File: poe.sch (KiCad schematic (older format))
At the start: 15 parts

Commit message: am Routing rumgespielt
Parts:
- 1.65k1, 1.65k2: renamed from 1.65kΩ; footprint (none) -> Resistors_ThroughHole:Resistor_Horizontal_RM20mm
- D1, D2: renamed from D?; footprint (none) -> Diodes_ThroughHole:Diode_DO-35_SOD27_Horizontal_RM10
- D10, D7, D8, D9: renamed from D?; footprint (none) -> LEDs:LED-3MM
- D3, D4, D5, D6: renamed from D?; footprint (none) -> Discret:D3
- P1: renamed from P?; footprint (none) -> Pin_Headers:Pin_Header_Angled_1x08
- R1, R2: renamed from R; footprint (none) -> Resistors_ThroughHole:Resistor_Horizontal_RM7mm
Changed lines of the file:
@@
 $EndDescr
 $Comp
-L CONN_01X08 P?
+L CONN_01X08 P1
 U 1 1 589CD597
 P 3300 3150
-F 0 "P?" H 3300 3600 50  0000 C CNN
+F 0 "P1" H 3300 3600 50  0000 C CNN
 F 1 "CONN_01X08" V 3400 3150 50  0000 C CNN
-F 2 "" H 3300 3150 50  0000 C CNN
+F 2 "Pin_Headers:Pin_Header_Angled_1x08" H 3300 3150 50  0001 C CNN
 F 3 "" H 3300 3150 50  0000 C CNN
 	1    3300 3150
@@
 $EndComp
 $Comp
-L R R
+L R R1
 U 1 1 589CD7AC
 P 5500 3050
-F 0 "R" V 5580 3050 50  0000 C CNN
+F 0 "R1" V 5580 3050 50  0000 C CNN
 F 1 "22kΩ" V 5500 3050 50  0000 C CNN
-F 2 "" V 5430 3050 50  0000 C CNN
+F 2 "Resistors_ThroughHole:Resistor_Horizontal_RM7mm" V 5430 3050 50  0001 C CNN
 F 3 "" H 5500 3050 50  0000 C CNN
 	1    5500 3050
@@
 $EndComp
 $Comp
-L R R
+L R R2
 U 1 1 589CD7FF
 P 5500 3800
-F 0 "R" V 5580 3800 50  0000 C CNN
+F 0 "R2" V 5580 3800 50  0000 C CNN
 F 1 "22kΩ" V 5500 3800 50  0000 C CNN
-F 2 "" V 5430 3800 50  0000 C CNN
+F 2 "Resistors_ThroughHole:Resistor_Horizontal_RM7mm" V 5430 3800 50  0001 C CNN
 F 3 "" H 5500 3800 50  0000 C CNN
 	1    5500 3800
@@
 $EndComp
 $Comp
-L ZENER D?
+L ZENER D4
 U 1 1 589CDF37
 P 5700 4000
-F 0 "D?" H 5700 4100 50  0000 C CNN
+F 0 "D4" H 5700 4100 50  0000 C CNN
 F 1 "ZENER" H 5700 3900 50  0000 C CNN
-F 2 "" H 5700 4000 50  0000 C CNN
+F 2 "Discret:D3" H 5700 4000 50  0001 C CNN
 F 3 "" H 5700 4000 50  0000 C CNN
 	1    5700 4000
@@
 $EndComp
 $Comp
-L ZENER D?
+L ZENER D6
 U 1 1 589CE16F
 P 6100 4000
-F 0 "D?" H 6100 4100 50  0000 C CNN
+F 0 "D6" H 6100 4100 50  0000 C CNN
 F 1 "ZENER" H 6100 3900 50  0000 C CNN
-F 2 "" H 6100 4000 50  0000 C CNN
+F 2 "Discret:D3" H 6100 4000 50  0001 C CNN
 F 3 "" H 6100 4000 50  0000 C CNN
 	1    6100 4000
@@
 $EndComp
 $Comp
-L ZENER D?
+L ZENER D3
 U 1 1 589CE1DE
 P 5700 2850
-F 0 "D?" H 5700 2950 50  0000 C CNN
+F 0 "D3" H 5700 2950 50  0000 C CNN
 F 1 "ZENER" H 5700 2750 50  0000 C CNN
-F 2 "" H 5700 2850 50  0000 C CNN
+F 2 "Discret:D3" H 5700 2850 50  0001 C CNN
 F 3 "" H 5700 2850 50  0000 C CNN
 	1    5700 2850
@@
 $EndComp
 $Comp
-L ZENER D?
+L ZENER D5
 U 1 1 589CE247
 P 6100 2850
-F 0 "D?" H 6100 2950 50  0000 C CNN
+F 0 "D5" H 6100 2950 50  0000 C CNN
 F 1 "ZENER" H 6100 2750 50  0000 C CNN
-F 2 "" H 6100 2850 50  0000 C CNN
+F 2 "Discret:D3" H 6100 2850 50  0001 C CNN
 F 3 "" H 6100 2850 50  0000 C CNN
 	1    6100 2850
@@
 $EndComp
 $Comp
-L R 1.65kΩ
+L R 1.65k1
 U 1 1 589CE2D4
 P 5750 3300
-F 0 "1.65kΩ" V 5830 3300 50  0000 C CNN
+F 0 "1.65k1" V 5830 3300 50  0000 C CNN
 F 1 "R" V 5750 3300 50  0000 C CNN
-F 2 "" V 5680 3300 50  0000 C CNN
+F 2 "Resistors_ThroughHole:Resistor_Horizontal_RM20mm" V 5680 3300 50  0001 C CNN
 F 3 "" H 5750 3300 50  0000 C CNN
 	1    5750 3300
@@
 $EndComp
 $Comp
-L R 1.65kΩ
+L R 1.65k2
 U 1 1 589CE307
 P 5750 3600
-F 0 "1.65kΩ" V 5830 3600 50  0000 C CNN
+F 0 "1.65k2" V 5830 3600 50  0000 C CNN
 F 1 "R" V 5750 3600 50  0000 C CNN
-F 2 "" V 5680 3600 50  0000 C CNN
+F 2 "Resistors_ThroughHole:Resistor_Horizontal_RM20mm" V 5680 3600 50  0001 C CNN
 F 3 "" H 5750 3600 50  0000 C CNN
 	1    5750 3600
@@
 $EndComp
 $Comp
-L LED D?
+L LED D8
 U 1 1 589CE453
 P 6300 3800
-F 0 "D?" H 6300 3900 50  0000 C CNN
+F 0 "D8" H 6300 3900 50  0000 C CNN
 F 1 "LED" H 6300 3700 50  0000 C CNN
-F 2 "" H 6300 3800 50  0000 C CNN
+F 2 "LEDs:LED-3MM" H 6300 3800 50  0001 C CNN
 F 3 "" H 6300 3800 50  0000 C CNN
 	1    6300 3800
@@
 $EndComp
 $Comp
-L LED D?
+L LED D10
 U 1 1 589CE49E
 P 6600 3800
-F 0 "D?" H 6600 3900 50  0000 C CNN
+F 0 "D10" H 6600 3900 50  0000 C CNN
 F 1 "LED" H 6600 3700 50  0000 C CNN
-F 2 "" H 6600 3800 50  0000 C CNN
+F 2 "LEDs:LED-3MM" H 6600 3800 50  0001 C CNN
 F 3 "" H 6600 3800 50  0000 C CNN
 	1    6600 3800
@@
 $EndComp
 $Comp
-L LED D?
+L LED D7
 U 1 1 589CE770
 P 6300 3050
-F 0 "D?" H 6300 3150 50  0000 C CNN
+F 0 "D7" H 6300 3150 50  0000 C CNN
 F 1 "LED" H 6300 2950 50  0000 C CNN
-F 2 "" H 6300 3050 50  0000 C CNN
+F 2 "LEDs:LED-3MM" H 6300 3050 50  0001 C CNN
 F 3 "" H 6300 3050 50  0000 C CNN
 	1    6300 3050
@@
 $EndComp
 $Comp
-L LED D?
+L LED D9
 U 1 1 589CE7ED
 P 6600 3050
-F 0 "D?" H 6600 3150 50  0000 C CNN
+F 0 "D9" H 6600 3150 50  0000 C CNN
 F 1 "LED" H 6600 2950 50  0000 C CNN
-F 2 "" H 6600 3050 50  0000 C CNN
+F 2 "LEDs:LED-3MM" H 6600 3050 50  0001 C CNN
 F 3 "" H 6600 3050 50  0000 C CNN
 	1    6600 3050
@@
 	6600 2850 6300 2850
 $Comp
-L Diode_Bridge D?
+L Diode_Bridge D1
 U 1 1 58A4AC46
 P 4600 2900
-F 0 "D?" H 4350 3200 50  0000 C CNN
+F 0 "D1" H 4350 3200 50  0000 C CNN
 F 1 "Diode_Bridge" H 4950 2550 50  0000 C CNN
-F 2 "" H 4600 2900 50  0000 C CNN
+F 2 "Diodes_ThroughHole:Diode_DO-35_SOD27_Horizontal_RM10" H 4600 2900 50  0001 C CNN
 F 3 "" H 4600 2900 50  0000 C CNN
 	1    4600 2900
@@
 	3600 3100 3600 3200
 $Comp
-L Diode_Bridge D?
+L Diode_Bridge D2
 U 1 1 58A4B96E
 P 4600 3800
-F 0 "D?" H 4350 4100 50  0000 C CNN
+F 0 "D2" H 4350 4100 50  0000 C CNN
 F 1 "Diode_Bridge" H 4950 3450 50  0000 C CNN
-F 2 "" H 4600 3800 50  0000 C CNN
+F 2 "Diodes_ThroughHole:Diode_DO-35_SOD27_Horizontal_RM10" H 4600 3800 50  0001 C CNN
 F 3 "" H 4600 3800 50  0000 C CNN
 	1    4600 3800

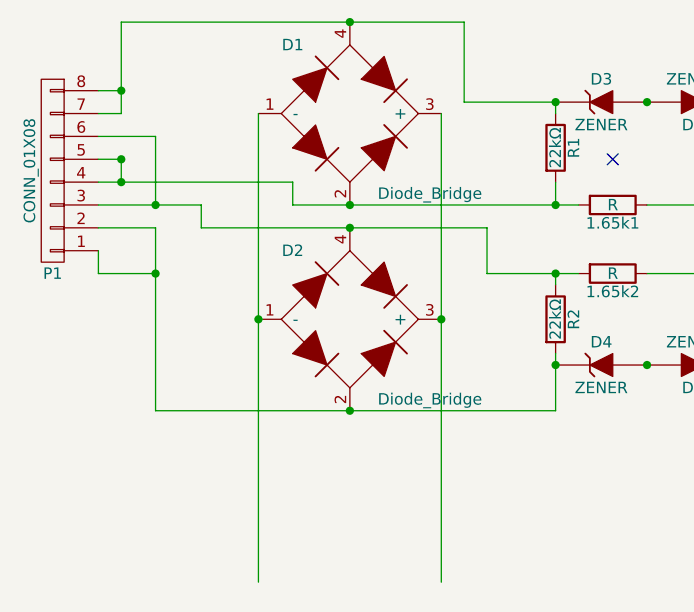
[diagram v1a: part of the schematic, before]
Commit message: Add NPN-MOSFET to output
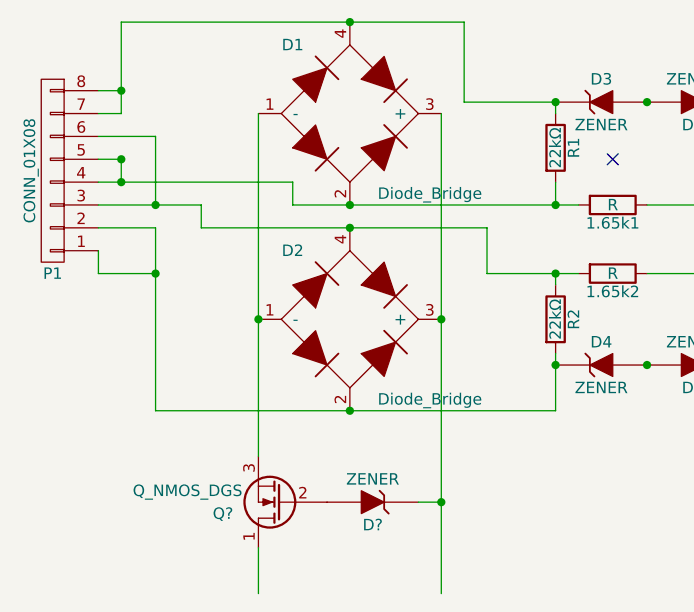
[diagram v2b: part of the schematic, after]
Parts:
- added D?: ZENER, symbol ZENER
- added Q?: Q_NMOS_DGS, symbol Q_NMOS_DGS
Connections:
- wire segments 35 -> 37
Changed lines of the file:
@@
 Wire Wire Line
 	3750 3600 3500 3600
-Wire Wire Line
-	4200 2900 4200 4950
-Wire Wire Line
-	5000 2900 5000 4950
 Connection ~ 4600 2500
 Connection ~ 4600 3300
@@
 Wire Wire Line
 	5500 3600 5500 3650
+$Comp
+L Q_NMOS_DGS Q?
+U 1 1 58B493A2
+P 4300 4600
+F 0 "Q?" H 4600 4650 50  0000 R CNN
+F 1 "Q_NMOS_DGS" H 4950 4550 50  0000 R CNN
+F 2 "" H 4500 4700 50  0000 C CNN
+F 3 "" H 4300 4600 50  0000 C CNN
+	1    4300 4600
+	-1   0    0    1
+$EndComp
+$Comp
+L ZENER D?
+U 1 1 58B4950D
+P 4700 4600
+F 0 "D?" H 4700 4700 50  0000 C CNN
+F 1 "ZENER" H 4700 4500 50  0000 C CNN
+F 2 "" H 4700 4600 50  0000 C CNN
+F 3 "" H 4700 4600 50  0000 C CNN
+	1    4700 4600
+	-1   0    0    1
+$EndComp
+Wire Wire Line
+	5000 4600 4900 4600
+Connection ~ 5000 4600
+Wire Wire Line
+	4200 4800 4200 5000
+Wire Wire Line
+	5000 2900 5000 5000
+Wire Wire Line
+	4200 2900 4200 4400
 $EndSCHEMATC

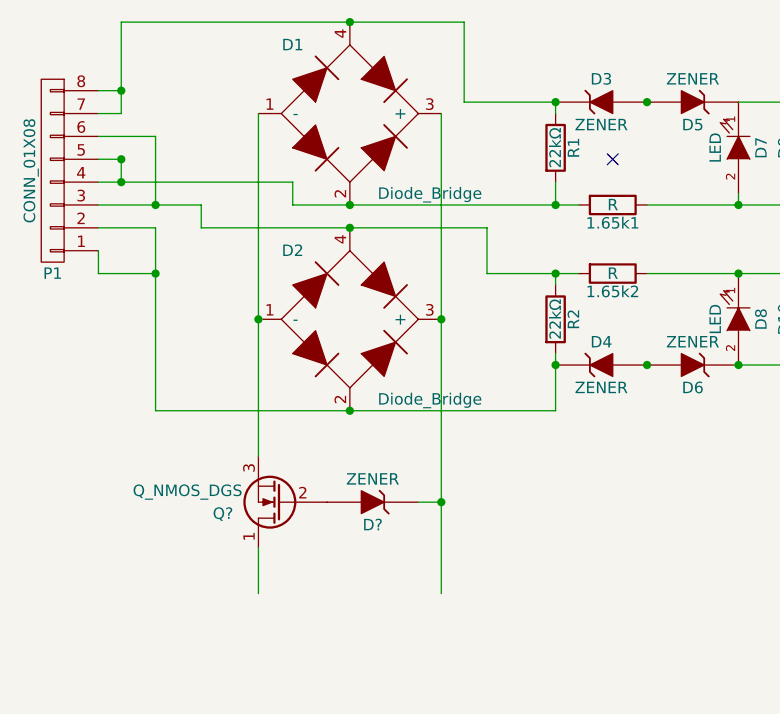
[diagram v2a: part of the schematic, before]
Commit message: +NMOS/Zener-enable load after classification
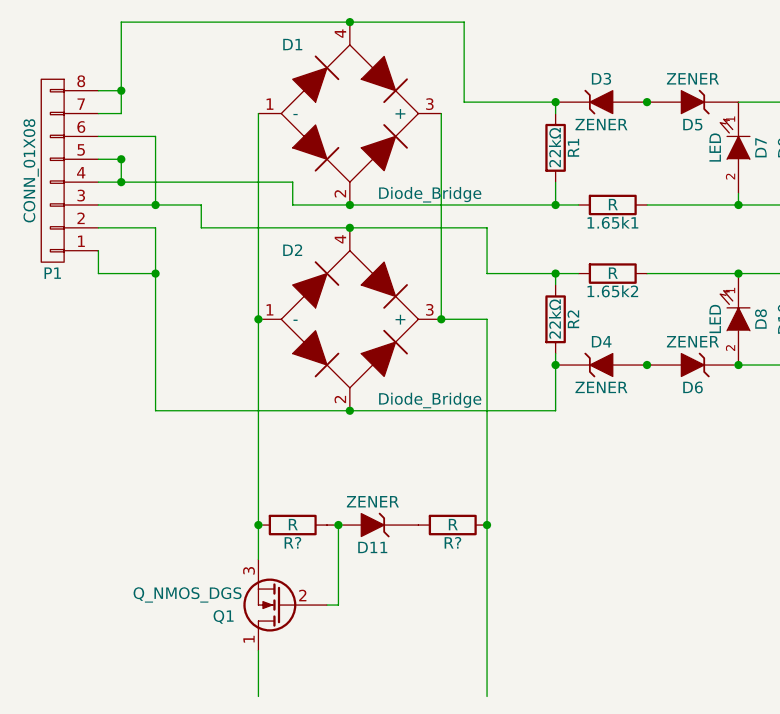
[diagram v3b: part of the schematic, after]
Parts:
- added R? (x2): R, symbol R
- gave numbers to parts that had none: 2
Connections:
- wire segments 37 -> 40
- no-connect marks 1 -> 0
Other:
- moved on the sheet: D11, Q1
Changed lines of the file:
@@
 Wire Wire Line
 	5200 3600 5200 3400
-NoConn ~ 5750 3100
 Wire Wire Line
 	5500 3300 5500 3200
@@
 	5500 3600 5500 3650
 $Comp
-L Q_NMOS_DGS Q?
+L Q_NMOS_DGS Q1
 U 1 1 58B493A2
-P 4300 4600
-F 0 "Q?" H 4600 4650 50  0000 R CNN
-F 1 "Q_NMOS_DGS" H 4950 4550 50  0000 R CNN
-F 2 "" H 4500 4700 50  0000 C CNN
-F 3 "" H 4300 4600 50  0000 C CNN
-	1    4300 4600
+P 4300 5050
+F 0 "Q1" H 4600 5100 50  0000 R CNN
+F 1 "Q_NMOS_DGS" H 4950 5000 50  0000 R CNN
+F 2 "" H 4500 5150 50  0000 C CNN
+F 3 "" H 4300 5050 50  0000 C CNN
+	1    4300 5050
 	-1   0    0    1
 $EndComp
 $Comp
-L ZENER D?
+L ZENER D11
 U 1 1 58B4950D
-P 4700 4600
-F 0 "D?" H 4700 4700 50  0000 C CNN
-F 1 "ZENER" H 4700 4500 50  0000 C CNN
-F 2 "" H 4700 4600 50  0000 C CNN
-F 3 "" H 4700 4600 50  0000 C CNN
-	1    4700 4600
+P 4700 4700
+F 0 "D11" H 4700 4800 50  0000 C CNN
+F 1 "ZENER" H 4700 4600 50  0000 C CNN
+F 2 "" H 4700 4700 50  0000 C CNN
+F 3 "" H 4700 4700 50  0000 C CNN
+	1    4700 4700
 	-1   0    0    1
 $EndComp
 Wire Wire Line
-	5000 4600 4900 4600
-Connection ~ 5000 4600
+	4200 5250 4200 5450
 Wire Wire Line
-	4200 4800 4200 5000
+	4200 2900 4200 4850
+$Comp
+L R R?
+U 1 1 58C46931
+P 4350 4700
+F 0 "R?" V 4430 4700 50  0000 C CNN
+F 1 "R" V 4350 4700 50  0000 C CNN
+F 2 "" V 4280 4700 50  0000 C CNN
+F 3 "" H 4350 4700 50  0000 C CNN
+	1    4350 4700
+	0    1    1    0
+$EndComp
+$Comp
+L R R?
+U 1 1 58C46A24
+P 5050 4700
+F 0 "R?" V 5130 4700 50  0000 C CNN
+F 1 "R" V 5050 4700 50  0000 C CNN
+F 2 "" V 4980 4700 50  0000 C CNN
+F 3 "" H 5050 4700 50  0000 C CNN
+	1    5050 4700
+	0    1    1    0
+$EndComp
 Wire Wire Line
-	5000 2900 5000 5000
+	5200 3800 5200 5450
 Wire Wire Line
-	4200 2900 4200 4400
+	5200 3800 5000 3800
+Wire Wire Line
+	5000 3800 5000 2900
+Wire Wire Line
+	4550 4700 4550 5050
+Wire Wire Line
+	4550 5050 4500 5050
+Connection ~ 5200 4700
+Connection ~ 4200 4700
+Connection ~ 4550 4700
 $EndSCHEMATC

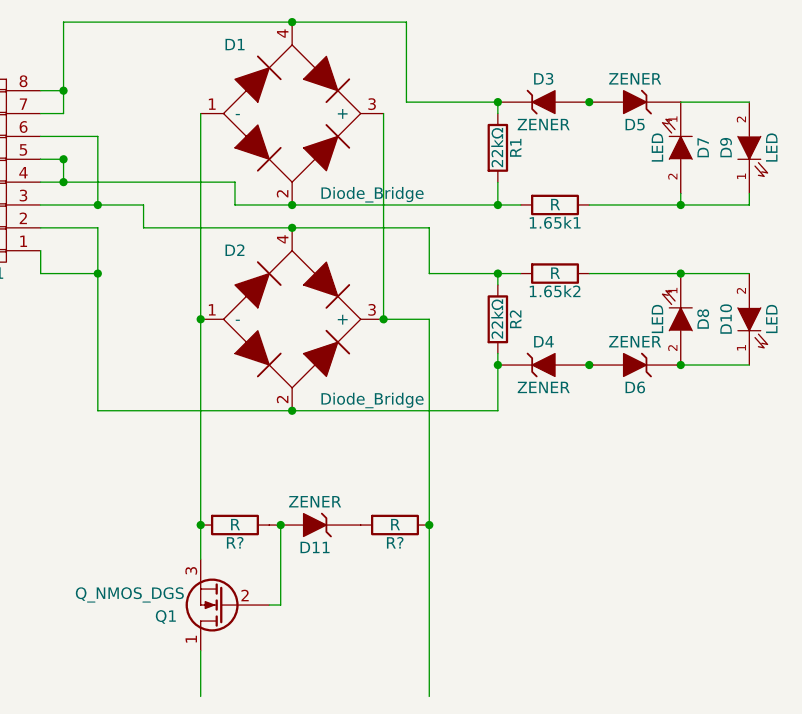
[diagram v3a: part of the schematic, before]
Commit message: widerstände vereinheitlicht
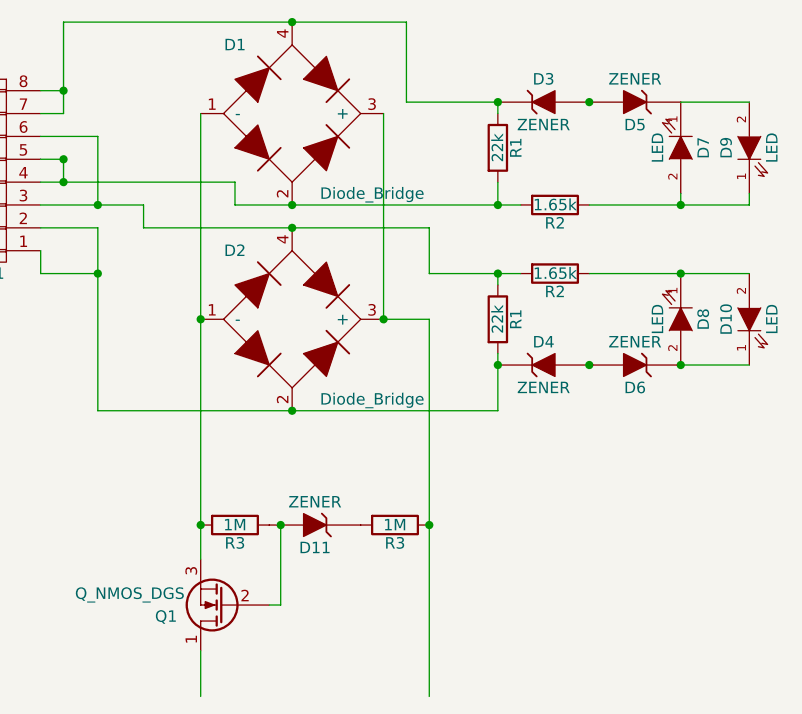
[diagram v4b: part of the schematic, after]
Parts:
- R1: value 22kΩ -> 22k
- R1: renamed from R2; value 22kΩ -> 22k
- R2: renamed from 1.65k1; value R -> 1.65k
- R2: renamed from 1.65k2; value R -> 1.65k
- R3: renamed from R?; value R -> 1M
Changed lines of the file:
@@
 P 5500 3050
 F 0 "R1" V 5580 3050 50  0000 C CNN
-F 1 "22kΩ" V 5500 3050 50  0000 C CNN
+F 1 "22k" V 5500 3050 50  0000 C CNN
 F 2 "Resistors_ThroughHole:Resistor_Horizontal_RM7mm" V 5430 3050 50  0001 C CNN
 F 3 "" H 5500 3050 50  0000 C CNN
@@
 $EndComp
 $Comp
-L R R2
+L R R1
 U 1 1 589CD7FF
 P 5500 3800
-F 0 "R2" V 5580 3800 50  0000 C CNN
-F 1 "22kΩ" V 5500 3800 50  0000 C CNN
+F 0 "R1" V 5580 3800 50  0000 C CNN
+F 1 "22k" V 5500 3800 50  0000 C CNN
 F 2 "Resistors_ThroughHole:Resistor_Horizontal_RM7mm" V 5430 3800 50  0001 C CNN
 F 3 "" H 5500 3800 50  0000 C CNN
@@
 $EndComp
 $Comp
-L R 1.65k1
+L R R2
 U 1 1 589CE2D4
 P 5750 3300
-F 0 "1.65k1" V 5830 3300 50  0000 C CNN
-F 1 "R" V 5750 3300 50  0000 C CNN
+F 0 "R2" V 5830 3300 50  0000 C CNN
+F 1 "1.65k" V 5750 3300 50  0000 C CNN
 F 2 "Resistors_ThroughHole:Resistor_Horizontal_RM20mm" V 5680 3300 50  0001 C CNN
 F 3 "" H 5750 3300 50  0000 C CNN
@@
 $EndComp
 $Comp
-L R 1.65k2
+L R R2
 U 1 1 589CE307
 P 5750 3600
-F 0 "1.65k2" V 5830 3600 50  0000 C CNN
-F 1 "R" V 5750 3600 50  0000 C CNN
+F 0 "R2" V 5830 3600 50  0000 C CNN
+F 1 "1.65k" V 5750 3600 50  0000 C CNN
 F 2 "Resistors_ThroughHole:Resistor_Horizontal_RM20mm" V 5680 3600 50  0001 C CNN
 F 3 "" H 5750 3600 50  0000 C CNN
@@
 	4200 2900 4200 4850
 $Comp
-L R R?
+L R R3
 U 1 1 58C46931
 P 4350 4700
-F 0 "R?" V 4430 4700 50  0000 C CNN
-F 1 "R" V 4350 4700 50  0000 C CNN
+F 0 "R3" V 4430 4700 50  0000 C CNN
+F 1 "1M" V 4350 4700 50  0000 C CNN
 F 2 "" V 4280 4700 50  0000 C CNN
 F 3 "" H 4350 4700 50  0000 C CNN
@@
 $EndComp
 $Comp
-L R R?
+L R R3
 U 1 1 58C46A24
 P 5050 4700
-F 0 "R?" V 5130 4700 50  0000 C CNN
-F 1 "R" V 5050 4700 50  0000 C CNN
+F 0 "R3" V 5130 4700 50  0000 C CNN
+F 1 "1M" V 5050 4700 50  0000 C CNN
 F 2 "" V 4980 4700 50  0000 C CNN
 F 3 "" H 5050 4700 50  0000 C CNN

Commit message: Stuff… Much Stuff…
(i know this commit is bad… but it would have been necessary ages ago)
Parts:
- removed D10, D9: LED, LEDs:LED-3MM, symbol LED
- removed P1: CONN_01X08, Pin_Headers:Pin_Header_Angled_1x08, symbol CONN_01X08
- removed Q1: Q_NMOS_DGS, symbol Q_NMOS_DGS
- added C1: >= 450 µF, Discret:C2V8, symbol CP
- added J1: RJ45, Connect:RJ45_8, symbol RJ45
- added P1: USB_A, Connect:USB_A, symbol USB_A
- added Q1: IRF640, pth-semi:TO-220, symbol IRF640
- added SW1: Switch_SPDT_x2, Custom:Switch, symbol Switch_SPDT_x2
- added U1: Step_Down, Custom:Step-Down, symbol Step_Down
- added U2, U3, U4, U5: Bananasocket, Custom:Bananasocket, symbol Bananasocket
- D1, D2: footprint Diodes_ThroughHole:Diode_DO-35_SOD27_Horizontal_RM10 -> Custom:Diode-Bridge
- D3: renamed from D11; footprint (none) -> Discret:D3
- R1, R2: renamed from R3; footprint (none) -> Resistors_ThroughHole:Resistor_Horizontal_RM7mm
- R5, R6: renamed from R2; value 1.65k -> 3.3k; footprint Resistors_ThroughHole:Resistor_Horizontal_RM20mm -> Resistors_ThroughHole:Resistor_Horizontal_RM7mm
- renumbered D3 to D4, D4 to D5, D5 to D6, D6 to D7, D7 to D8, D8 to D9, R1 to R3, R1 to R4
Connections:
- net labels added: Earth, Ethernet+, Ethernet-, GND, VDD
- wire segments 40 -> 56
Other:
- moved on the sheet: D3, R2
